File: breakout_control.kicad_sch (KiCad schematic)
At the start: 6 parts, among them J11 Conn_01x03_MountingPin, U47 TXB0104PW

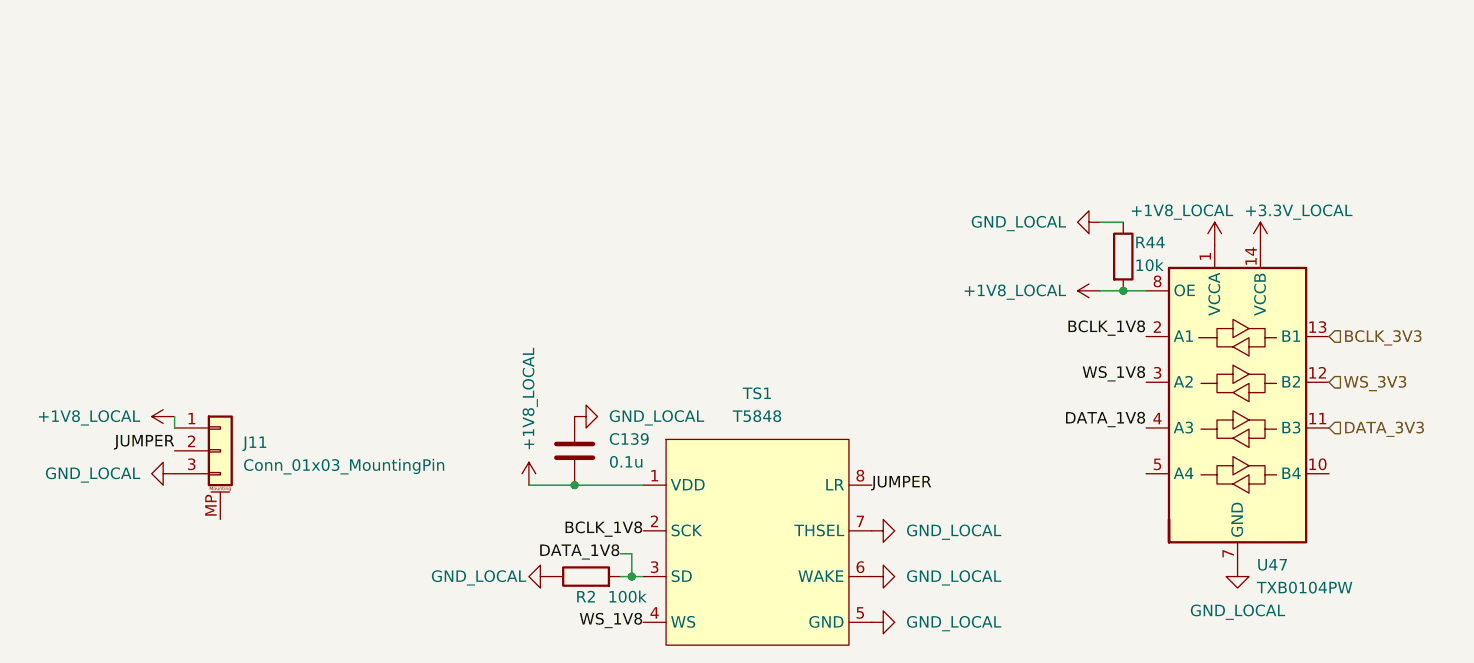
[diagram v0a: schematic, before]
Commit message: Fixed most ERC checks
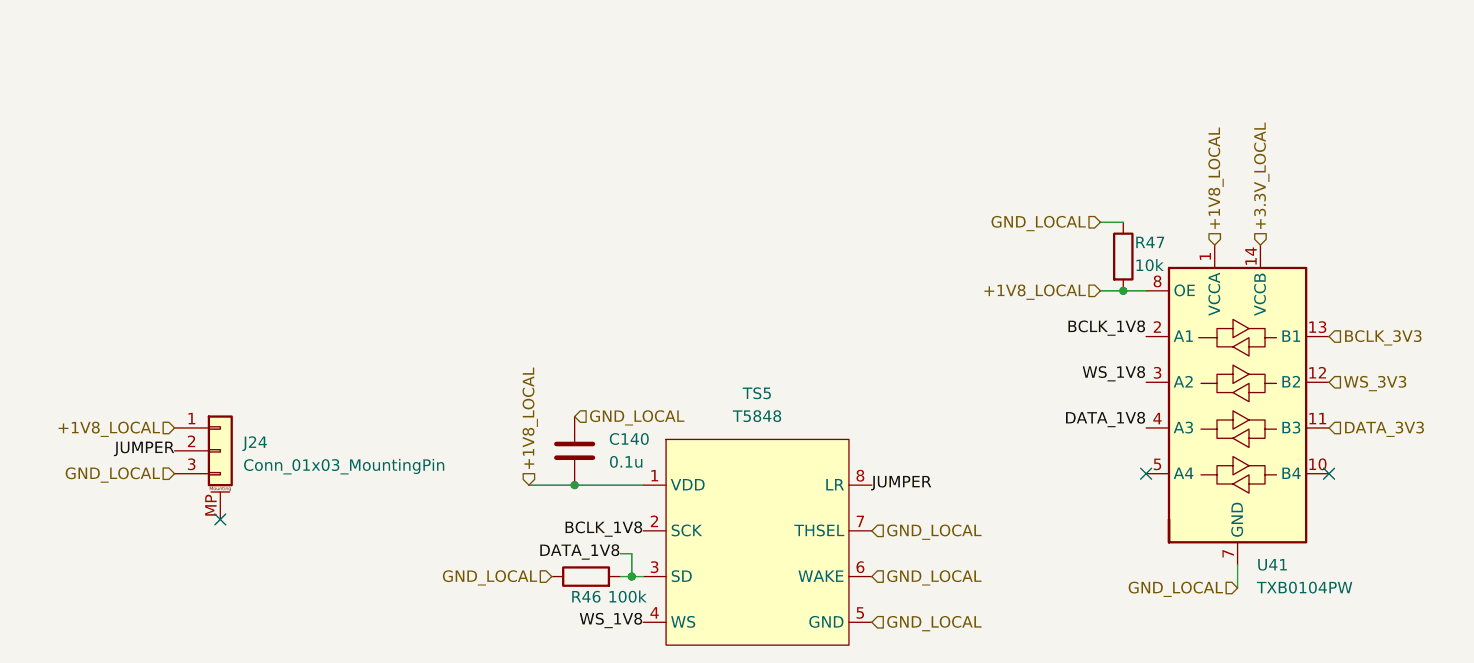
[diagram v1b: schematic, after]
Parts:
- renumbered C139 to C140, J11 to J24, R2 to R46, R44 to R47, TS1 to TS5, U47 to U41
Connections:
- no-connect marks 0 -> 3

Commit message: Footprinting done (warnings on schematic side but pcb import works fine)
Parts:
- C140: footprint (none) -> Capacitor_SMD:C_0603_1608Metric
- J24: footprint (none) -> Connector_PinHeader_2.54mm:PinHeader_1x03_P2.54mm_Vertical_SMD_Pin1Left; LCSC Part # (none) -> C5160786
- R46, R47: footprint (none) -> Resistor_SMD:R_0603_1608Metric
- TS5: footprint (none) -> T5848:TDK_T5848_Pad
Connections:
- no-connect marks 3 -> 2
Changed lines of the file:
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@@
 		(at 223.52 66.04)
-	)
-	(no_connect
-		(at 100.33 71.12)
 	)
 	(wire
@@
 			)
 		)
-		(property "Footprint" ""
+		(property "Footprint" "Capacitor_SMD:C_0603_1608Metric"
 			(at 138.7348 59.69 0)
 			(effects
@@
 			)
 		)
-		(property "Footprint" ""
+		(property "Footprint" "Resistor_SMD:R_0603_1608Metric"
 			(at 140.97 79.248 90)
 			(effects
@@
 			)
 		)
-		(property "Footprint" ""
+		(property "Footprint" "Resistor_SMD:R_0603_1608Metric"
 			(at 198.882 41.91 90)
 			(effects
@@
 			)
 		)
-		(property "Footprint" ""
+		(property "Footprint" "T5848:TDK_T5848_Pad"
 			(at 160.02 63.5 0)
 			(effects
@@
 			)
 		)
-		(property "Footprint" ""
+		(property "Footprint" "Connector_PinHeader_2.54mm:PinHeader_1x03_P2.54mm_Vertical_SMD_Pin1Left"
 			(at 100.33 63.5 0)
 			(effects
@@
 			)
 		)
+		(property "LCSC Part #" "C5160786"
+			(at 100.33 63.5 0)
+			(effects
+				(font
+					(size 1.27 1.27)
+				)
+				(hide yes)
+			)
+		)
 		(pin "2"
 		)
@@
 		(pin "1"
 		)
-		(pin "MP"
-		)
 		(instances

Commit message: Minor schematic changes
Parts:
- added C289, C291: 0.1u, Capacitor_SMD:C_0603_1608Metric, symbol Device:C
- renumbered C140 to C287, J24 to J15, R46 to R90, R47 to R92, U41 to U53
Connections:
- net +1V8_LOCAL: now also C289.2
- net +3.3V_LOCAL: now also C291.1
- net GND_LOCAL: now also C289.1, C291.2
